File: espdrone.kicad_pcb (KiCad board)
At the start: 6 copper layers, 60 x 60 mm, 508 parts, among them J1 Conn_01x06, J10 Conn_01x04, J11 Conn_01x04, J12 Conn_01x04, J2 Conn_01x04, J3 Conn_01x14, J4 Conn_01x06, J5 Conn_Coaxial, J7 Conn_01x06, J8 Conn_01x04, J9 Conn_01x04, Q1 NMOS, Q10 NMOS, Q11 NMOS, Q12 NMOS, Q13 NMOS, Q14 NMOS, Q15 NMOS, Q16 NMOS, Q17 NMOS, Q18 NMOS, Q19 NMOS, Q2 NMOS, Q20 NMOS, Q21 NMOS, Q22 NMOS, Q23 NMOS, Q24 NMOS, Q25 NMOS, Q26 NMOS, Q27 NMOS, Q28 NMOS, Q3 NMOS, Q4 NMOS, Q5 NMOS, Q6 NMOS, Q7 NMOS, Q8 NMOS, Q9 NMOS, U10 FPC-1.0FX-15PWCR-H20, U11 VL53L1CXV0FY1, U12 LIS2MDL, U13 LSM6DS3, U14 PMW3901MB-TXQT_C43496881, U15 STM32G071K8U6, U16 DRV8328ARUYR, U17 INA180A2, U18 STM32G071K8U6, U19 DRV8328ARUYR, U2 USBLC6-2P6, U20 INA180A2, U21 STM32G071K8U6, U22 DRV8328ARUYR, U23 INA180A2, U24 STM32G071K8U6, U25 DRV8328ARUYR, U26 INA180A2, U3 W25Q128JVP, U4 ESP32-C5HF4, U5 LFD182G45DCHD277, U6 TLV62569DBV, U7 XC6206P182MR_C347373, U8 TPS63070RNMR, U9 TPS2121RUXR, Y1 Crystal_GND24, Y2 Crystal_GND24

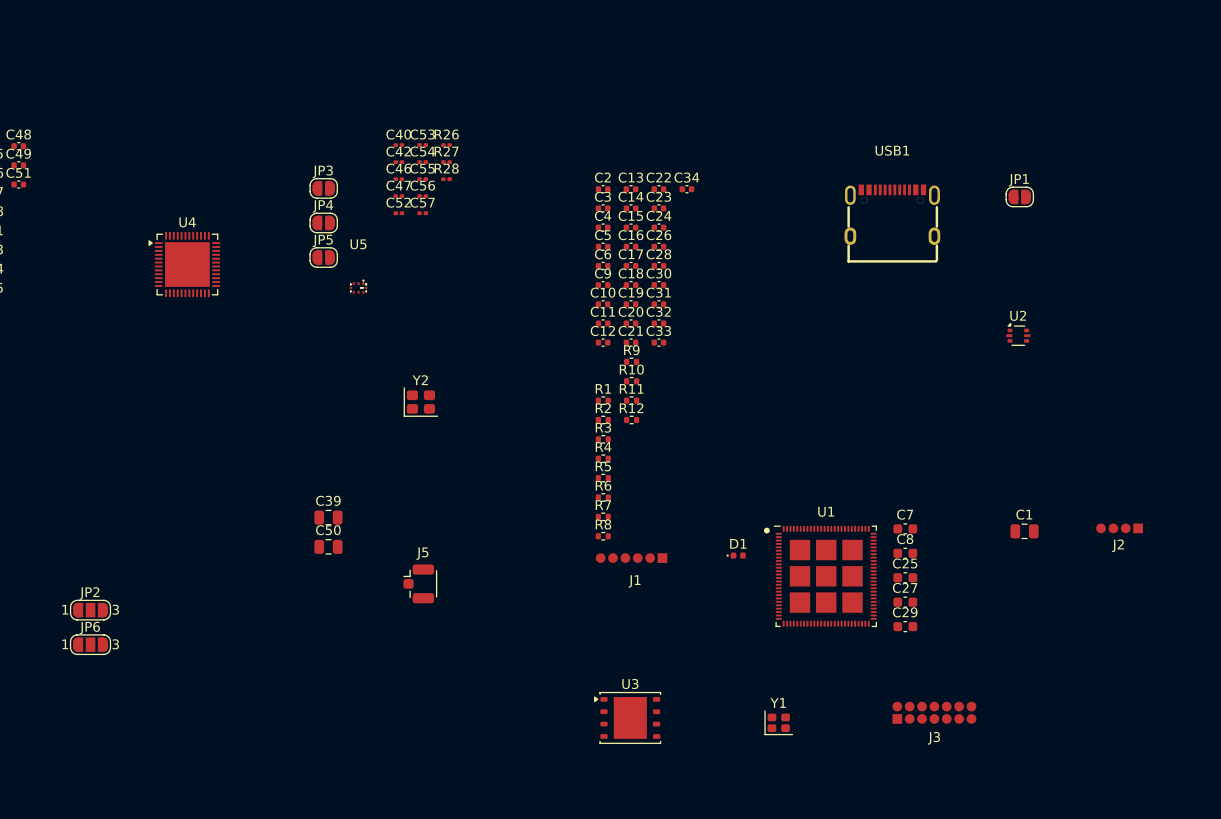
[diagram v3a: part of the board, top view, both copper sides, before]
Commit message: Add custom solder jumper footprint, begin layouting
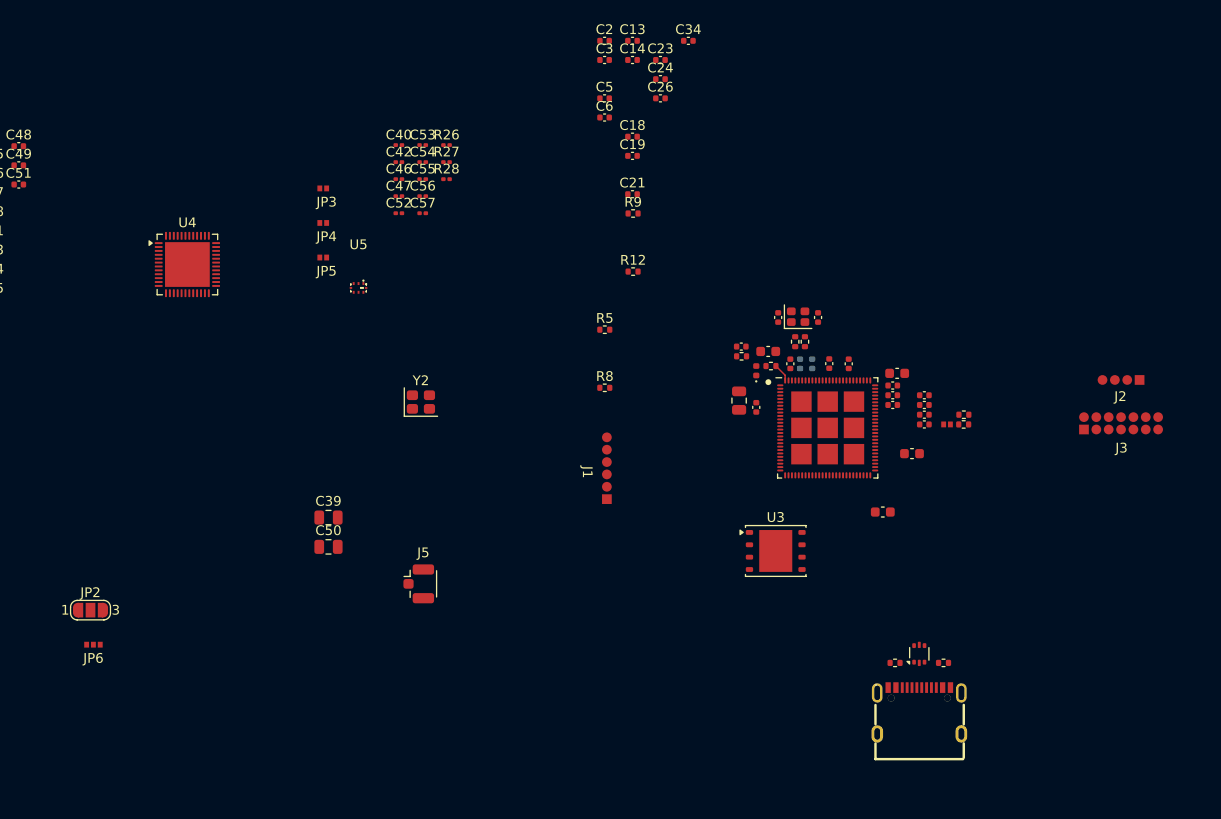
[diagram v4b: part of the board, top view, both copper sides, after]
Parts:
- C15, C9: moved to B.Cu
- C7: value 1u -> 100n; footprint Capacitor_SMD:C_0603_1608Metric -> Capacitor_SMD:C_0402_1005Metric
- JP1, JP3, JP4, JP5: footprint Jumper:SolderJumper-2_P1.3mm_Open_RoundedPad1.0x1.5mm -> easyeda2kicad:SolderJumper-2-0.6x0.5mm
- JP6: footprint Jumper:SolderJumper-3_P1.3mm_Open_RoundedPad1.0x1.5mm_NumberLabels -> easyeda2kicad:SolderJumper-3-0.6x0.5mm_1
- moved USB1 51.2 mm to (169.8, 3.17)
- moved R11 41.9 mm to (172.2, -1.75)
- moved Y1 41.8 mm to (157.3, -37.3)
- moved R10 39.6 mm to (167.3, -1.75), turned to 180 degrees
- moved R7 38.2 mm to (174.3, -26.2)
- moved R6 38.0 mm to (174.3, -27.2)
- moved J3 35.4 mm to (190.5, -23.3)
- moved U2 34.2 mm to (169.8, -2.67), turned to 90 degrees
- moved C1 32.3 mm to (151.2, -28.7), turned to 90 degrees
- moved C22 31.4 mm to (167.0, -30.2)
- moved C30 30.8 mm to (170.3, -26.2)
- moved C31 29.5 mm to (170.3, -27.2)
- moved C32 28.5 mm to (170.3, -28.2)
- moved C28 27.9 mm to (167.0, -28.2)
- moved C20 27.9 mm to (167.0, -29.2)
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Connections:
- net /Motors/ESC1/A renamed /Motors/ESC1/PHASE_A
- net /Motors/ESC1/B renamed /Motors/ESC1/PHASE_B
- net /Motors/ESC1/C renamed /Motors/ESC1/PHASE_C
- net /Motors/ESC2/A renamed /Motors/ESC2/PHASE_A
- net /Motors/ESC2/B renamed /Motors/ESC2/PHASE_B
- net /Motors/ESC2/C renamed /Motors/ESC2/PHASE_C
- net /Motors/ESC3/A renamed /Motors/ESC3/PHASE_A
- net /Motors/ESC3/B renamed /Motors/ESC3/PHASE_B
- net /Motors/ESC3/C renamed /Motors/ESC3/PHASE_C
- net /Motors/ESC4/A renamed /Motors/ESC4/PHASE_A
- net /Motors/ESC4/B renamed /Motors/ESC4/PHASE_B
- net /Motors/ESC4/C renamed /Motors/ESC4/PHASE_C
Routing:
- net Net-(U1-GPIO0): track 0.00 -> 1.87 mm
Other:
- board text added: "MIPI spacing: 0.10mm within pair, 0.3mm to unrelated copper, 0.5mm between pairs"

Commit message: Reduce amounts of broken out GPIOs
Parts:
- removed J1: Conn_01x06, easyeda2kicad:Connector_Pad_1.27mm_1x06
- removed J2: Conn_01x04, easyeda2kicad:Connector_Pad_1.27mm_1x04
- removed J3: Conn_01x14, easyeda2kicad:Connector_pad_1.27mm_2x07
- added J6: Conn_01x06, easyeda2kicad:Connector_Pad_1.27mm_1x06, F.Cu at (174.4, -27.8)
- moved C13 50.0 mm to (160.0, -19.8), turned to 180 degrees
- moved C14 49.1 mm to (160.0, -18.8), turned to 180 degrees
- moved C34 47.3 mm to (157.5, -19.8)
- moved C23 46.5 mm to (167.0, -23.8)
- moved C24 46.3 mm to (167.0, -22.0)
- moved C3 45.5 mm to (153.8, -21.2), turned to 180 degrees
- moved C2 45.4 mm to (153.7, -23.2), turned to 180 degrees
- moved C6 44.5 mm to (157.8, -18.2), turned to -90 degrees
- moved C5 43.9 mm to (155.5, -19.8), turned to 180 degrees
- moved C18 42.9 mm to (160.0, -17.8), turned to 180 degrees
- moved C19 42.3 mm to (165.3, -19.8)
- moved C26 41.1 mm to (167.0, -26.2)
- moved R9 40.4 mm to (176.0, -29.0), turned to 90 degrees
- moved C21 40.0 mm to (165.3, -18.8)
- moved R8 38.6 mm to (176.0, -31.0), turned to 90 degrees
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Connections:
- U1 pad 2: /MCU/P4_MTCK -> unconnected-(U1-GPIO2-Pad2)
- U1 pad 3: /MCU/P4_MTDI -> unconnected-(U1-GPIO3-Pad3)
- U1 pad 4: /MCU/P4_MTMS -> unconnected-(U1-GPIO4-Pad4)
- U1 pad 5: /MCU/P4_MTDO -> unconnected-(U1-GPIO5-Pad5)
- U1 pad 57: /MCU/GPIO28 -> unconnected-(U1-GPIO28-Pad57)
- U1 pad 58: /MCU/GPIO29 -> unconnected-(U1-GPIO29-Pad58)
- U1 pad 6: /MCU/GPIO6 -> unconnected-(U1-GPIO6-Pad6)
- U1 pad 60: /MCU/GPIO30 -> unconnected-(U1-GPIO30-Pad60)
- U1 pad 61: /MCU/GPIO31 -> unconnected-(U1-GPIO31-Pad61)
- U1 pad 63: /MCU/GPIO32 -> unconnected-(U1-GPIO32-Pad63)
- U1 pad 64: /MCU/GPIO33 -> unconnected-(U1-GPIO33-Pad64)
- U1 pad 65: /MCU/GPIO34 -> unconnected-(U1-GPIO34-Pad65)
- U1 pad 92: /MCU/GPIO49 -> unconnected-(U1-GPIO49/ADC2_CHANNEL0-Pad92)
- U1 pad 93: /MCU/GPIO50 -> unconnected-(U1-GPIO50/ADC2_CHANNEL1-Pad93)

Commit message: Sort of workable P4 layout
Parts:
- C1, C10, C13, C14, C16, C17, C18, C19, C20, C21, C22, C23, C24, C25, C26, C27, C28, C29, C4, C8: moved to B.Cu
- moved J6 138.0 mm to (111.6, 95.0)
- moved R8 138.0 mm to (113.1, 91.8)
- moved R9 138.0 mm to (113.1, 93.8)
- moved R7 137.9 mm to (113.2, 97.3), turned to -90 degrees
- moved R6 137.6 mm to (110.4, 94.6)
- moved C16 136.4 mm to (103.9, 91.6), turned to -90 degrees
- moved C17 136.4 mm to (105.9, 91.6), turned to -90 degrees
- moved C10 136.3 mm to (100.2, 91.6), turned to -90 degrees
- moved C15 136.3 mm to (102.4, 91.6), turned to -90 degrees
- moved C9 136.3 mm to (101.2, 91.6), turned to -90 degrees
- moved C27 135.7 mm to (106.7, 89.8), turned to 180 degrees
- moved JP1 135.7 mm to (113.2, 95.7), turned to -90 degrees
- moved C22 135.5 mm to (107.7, 91.6), turned to -90 degrees
- moved C11 134.6 mm to (98.7, 84.9)
- moved C12 134.6 mm to (102.8, 84.9)
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
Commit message: Preliminary C5 layout done
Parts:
- removed R15, R24: 10k, Resistor_SMD:R_0402_1005Metric
- C37: value 1u -> 100n
- C38, C39, C41, C43, C44, C45, C49, C50, C51: moved to B.Cu
- C64, C69: footprint Capacitor_SMD:C_0805_2012Metric -> Capacitor_SMD:C_0603_1608Metric
- JP2: footprint Jumper:SolderJumper-3_P1.3mm_Open_RoundedPad1.0x1.5mm_NumberLabels -> easyeda2kicad:SolderJumper-3-0.6x0.5mm_1
- R100, R101, R102, R103, R104, R105, R108, R109, R110, R125, R126, R127, R128, R129, R130, R133, R134, R135, R150, R151, R152, R153, R154, R155, R158, R159, R160, R75, R76, R77, R78, R79, R80, R83, R84, R85: footprint Resistor_SMD:R_0603_1608Metric -> Resistor_SMD:R_0402_1005Metric
- moved U10 157.6 mm to (105.5, 120.4)
- moved C35 140.0 mm to (98.3, 85.0), turned to 180 degrees
- moved C40 138.3 mm to (101.3, 82.5), turned to 180 degrees
- moved C49 137.9 mm to (105.0, 82.2), turned to -90 degrees
- moved D2 137.6 mm to (241.1, 112.8), turned to 180 degrees
- moved C51 136.2 mm to (106.0, 82.2), turned to -90 degrees
- moved C37 136.1 mm to (101.0, 84.5), turned to 180 degrees
- moved C42 135.8 mm to (101.3, 81.8), turned to 180 degrees
- moved C48 135.5 mm to (108.1, 77.0), turned to 90 degrees
- moved C53 135.2 mm to (105.7, 79.6), turned to 180 degrees
- moved R26 134.6 mm to (103.5, 78.5), turned to 90 degrees
- moved C38 134.1 mm to (104.3, 83.8)
- moved U8 133.9 mm to (244.6, 104.7)
- moved C36 133.3 mm to (98.3, 80.3)
- moved C41 133.2 mm to (104.3, 84.8)
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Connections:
- JP2 pad 1: Net-(JP2-A) -> +3V3
- JP2 pad 2: Net-(J4-Pin_4) -> Net-(JP2-C)
- JP2 pad 3: Net-(JP2-B) -> GND
- JP3 pad 1: Net-(JP3-A) -> GND
- JP4 pad 2: Net-(JP4-B) -> GND
- JP5 pad 2: Net-(JP5-B) -> GND
- JP6 pad 1: Net-(JP6-A) -> GND
- JP6 pad 3: Net-(JP6-B) -> +3V3
- R13 pad 1: Net-(JP2-A) -> Net-(J4-Pin_3)
- R13 pad 2: +3V3 -> Net-(JP2-C)
- R18 pad 1: Net-(JP6-A) -> Net-(JP6-C)
- R18 pad 2: +3V3 -> Net-(U4-GPIO25)
- R20 pad 1: Net-(JP3-A) -> Net-(U4-GPIO26)
- R20 pad 2: GND -> Net-(JP3-B)
- R21 pad 1: Net-(JP4-B) -> Net-(U4-GPIO27)
- R21 pad 2: GND -> Net-(JP4-A)
- R22 pad 1: Net-(JP5-B) -> Net-(U4-GPIO28)
- R22 pad 2: GND -> Net-(JP5-A)
- U4 pad 1: GND -> +3V3
- U4 pad 11: Net-(J4-Pin_3) -> Net-(J4-Pin_2)
- U4 pad 12: Net-(J4-Pin_4) -> Net-(J4-Pin_3)
- U4 pad 13: Net-(J4-Pin_5) -> Net-(J4-Pin_4)
- U4 pad 14: Net-(J4-Pin_2) -> Net-(J4-Pin_5)
- U4 pad 3: GND -> +3V3
- U4 pad 35: Net-(JP6-C) -> Net-(U4-GPIO25)
- U4 pad 36: Net-(JP3-B) -> Net-(U4-GPIO26)
- U4 pad 37: Net-(JP4-A) -> Net-(U4-GPIO27)
- U4 pad 38: Net-(JP5-A) -> Net-(U4-GPIO28)
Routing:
- added copper zone on In2.Cu, net +3V3
- added copper zone on In3.Cu, net +BATT
- added copper zone on In1.Cu, net GND
- added copper zone on In4.Cu, net GND
